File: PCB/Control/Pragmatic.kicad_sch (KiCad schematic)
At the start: 4 parts, among them J1 L, J2 R, SW1 SW_Push, U1 ProMicro

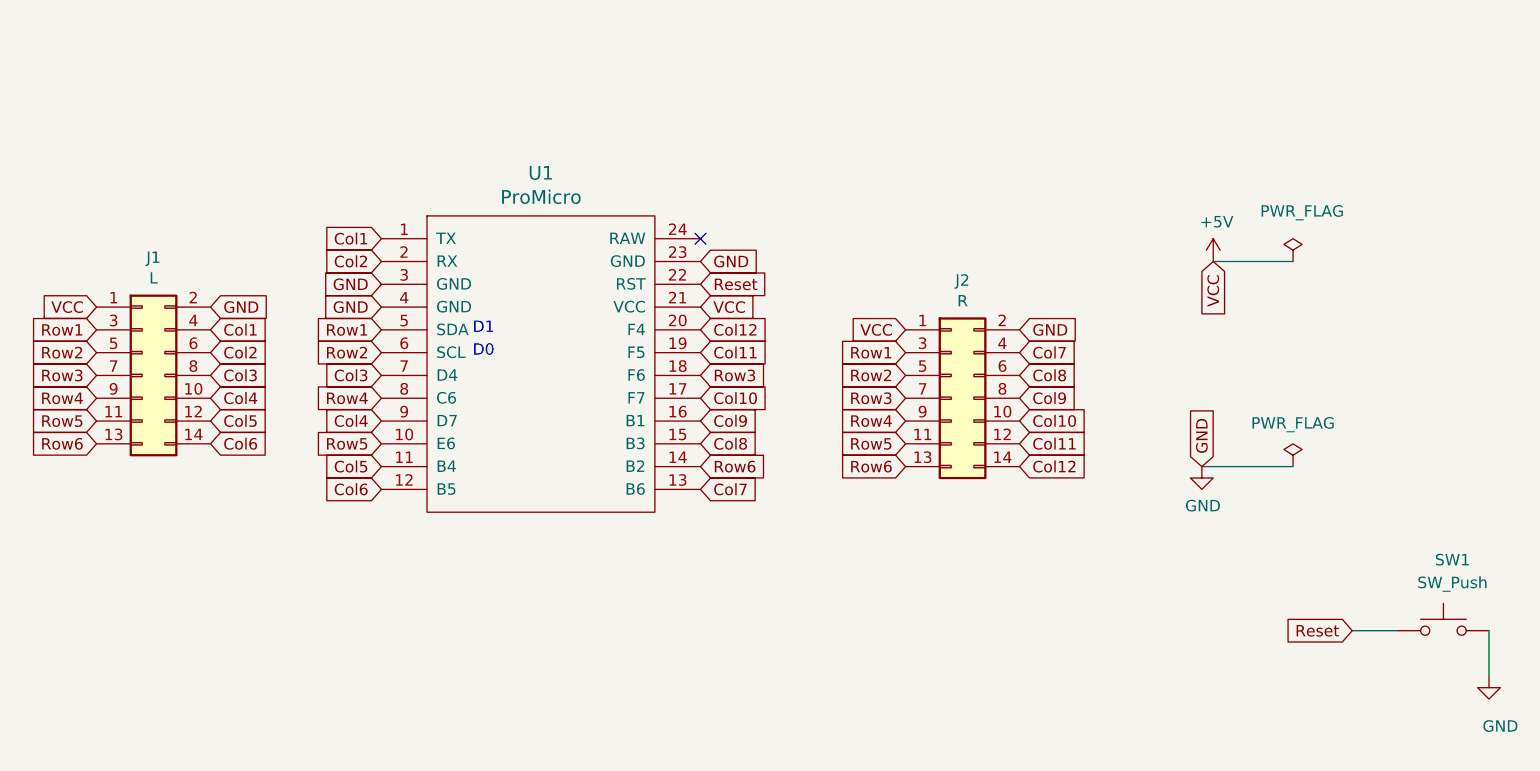
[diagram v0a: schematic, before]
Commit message: add elite C extension
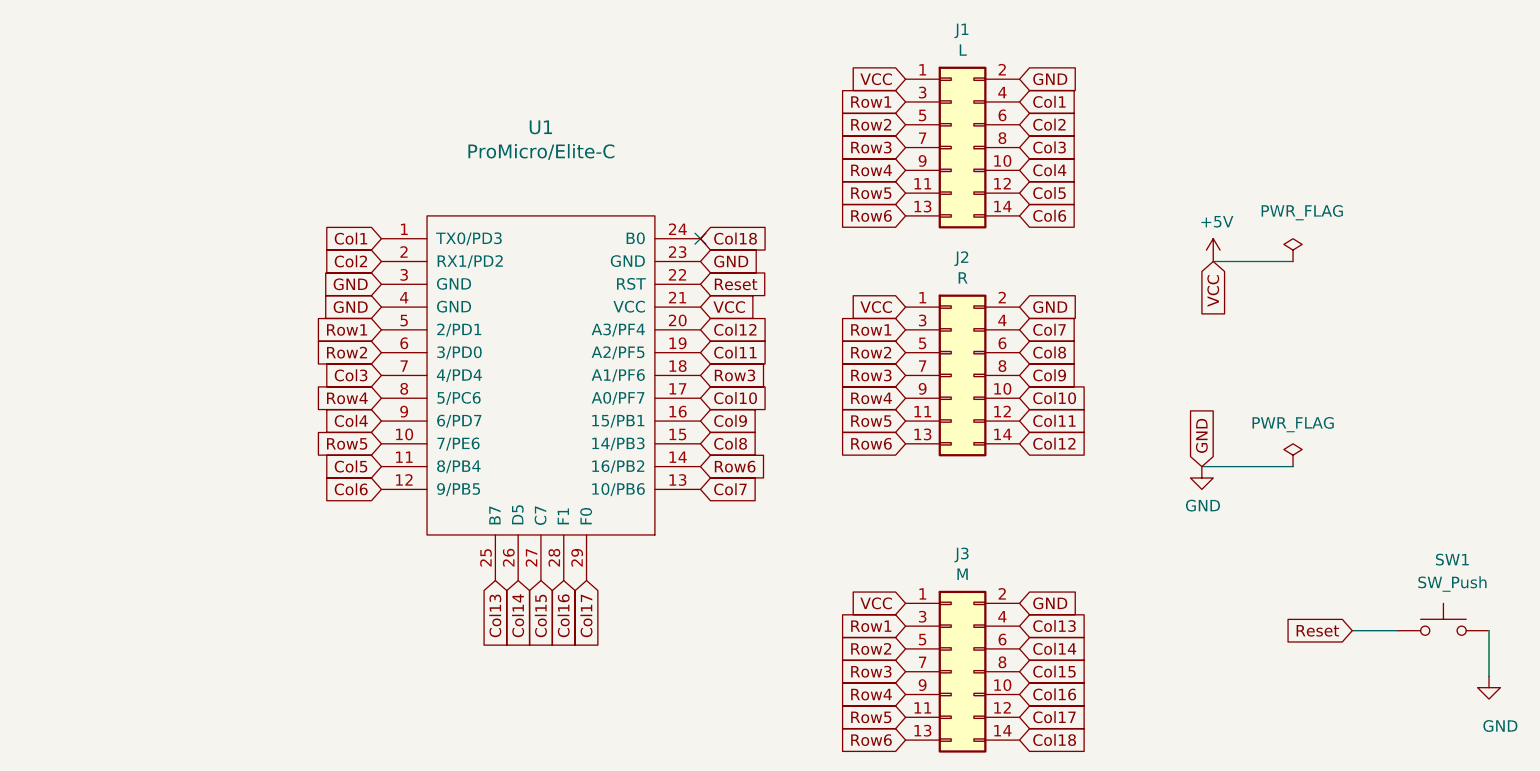
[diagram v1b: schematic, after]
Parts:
- added J3: M, Connector_IDC:IDC-Header_2x07_P2.54mm_Vertical, symbol Connector_Generic:Conn_02x07_Odd_Even
- U1: value ProMicro -> ProMicro/Elite-C; footprint keyboards:ArduinoProMicro -> Keyboard_Keebio-Parts:Elite-C; symbol Biacco42:ProMicro -> Keyboard_Keebio:Elite-C
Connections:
- net +5V: now also J3.1 (Pin_1)
- net GND: now also J3.2 (Pin_2)
- net Row1: now also J3.3 (Pin_3)
- net Row2: now also J3.5 (Pin_5)
- net Row3: now also J3.7 (Pin_7)
- net Row4: now also J3.9 (Pin_9)
- net Row5: now also J3.11 (Pin_11)
- net Row6: now also J3.13 (Pin_13)
- net Col18: now reaches U1.24 (B0)
- net Col18: now also J3.14 (Pin_14)
- new net Col13: J3.4 (Pin_4), U1.25 (B7)
- new net Col14: J3.6 (Pin_6), U1.26 (D5)
- new net Col15: J3.8 (Pin_8), U1.27 (C7)
- new net Col16: J3.10 (Pin_10), U1.28 (F1)
- new net Col17: J3.12 (Pin_12), U1.29 (F0)
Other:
- note removed: "D0"
- note removed: "D1"
- moved on the sheet: J1, J2
